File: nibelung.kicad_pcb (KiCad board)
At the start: 2 copper layers, 35.6 x 35.6 mm, 48 parts, among them J1 JST_PH_01x02, J2 JST_PH_01x02, J3 AudioJack3-TSW, J4 ScrewTerm_01x08_2.54mm, J5 ScrewTerm_01x08_2.54mm, J6 JST_SH_01x03, J7 JST_SH_01x03, U1 74HCT245, U2 LTC2850xS8, U3 Teensy4.0

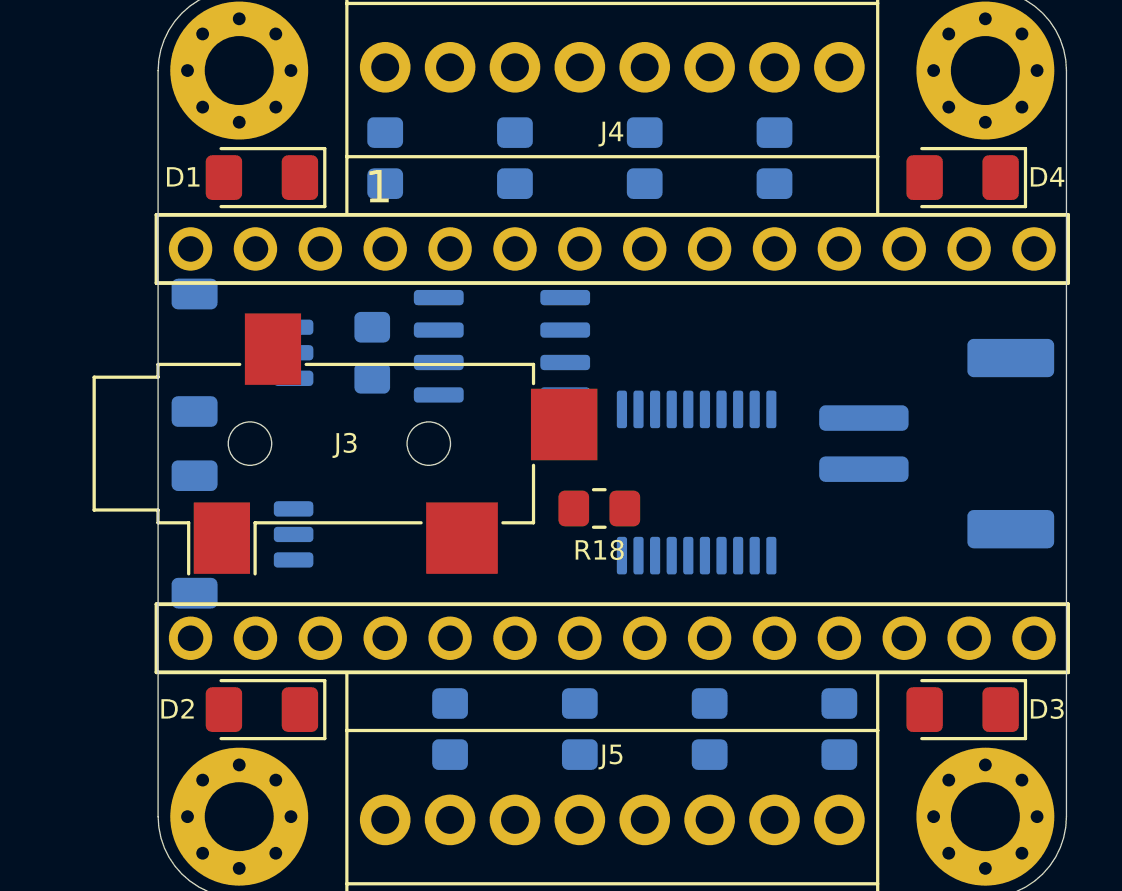
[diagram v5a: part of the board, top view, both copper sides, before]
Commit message: Revise placement and label output connections
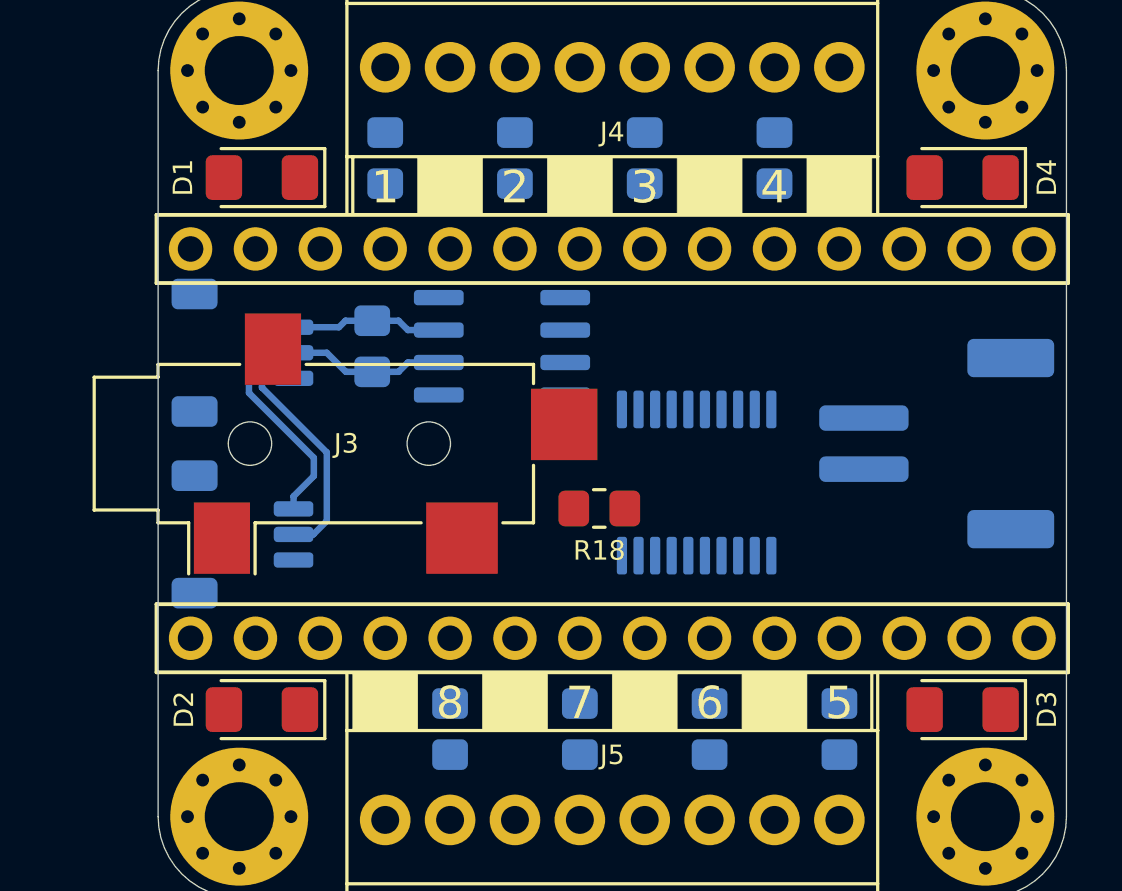
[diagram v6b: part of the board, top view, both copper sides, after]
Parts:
- moved R1 0.25 mm to (111.3, 97.8)
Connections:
- J6 pad 1: /A -> GND
- J6 pad 2: GND -> /A
- J7 pad 1: /A -> GND
- J7 pad 2: GND -> /A
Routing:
- net /A: track 0.00 -> 16.4 mm
- net /B: track 0.00 -> 15.7 mm
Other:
- net class Minimum added: clearance 0.1524, trace_width 0.1524, via_dia 0.508, via_drill 0.254
- net class Thin added: clearance 0.2032, trace_width 0.2032, via_dia 0.6096, via_drill 0.3048
- board text added: "2"
- board text added: "3"
- board text added: "4"
- board text added: "5"
- board text added: "6"
- board text added: "7"
- board text added: "8"
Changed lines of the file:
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@@
   (general
     (thickness 1.6)
-    (drawings 19)
-    (tracks 0)
+    (drawings 44)
+    (tracks 26)
     (zones 0)
     (modules 48)
@@
   (setup
     (last_trace_width 0.254)
+    (user_trace_width 0.1524)
+    (user_trace_width 0.2032)
+    (user_trace_width 0.254)
+    (user_trace_width 0.508)
+    (user_trace_width 0.635)
+    (user_trace_width 0.762)
+    (user_trace_width 1.27)
     (trace_clearance 0.254)
     (zone_clearance 0.508)
@@
     (via_min_size 0.508)
     (via_min_drill 0.254)
-    (uvia_size 0.6096)
-    (uvia_drill 0.3048)
+    (user_via 0.508 0.254)
+    (user_via 0.6096 0.3048)
+    (user_via 0.762 0.381)
+    (user_via 1.016 0.508)
+    (uvia_size 0.762)
+    (uvia_drill 0.381)
     (uvias_allowed no)
     (uvia_min_size 0)
@@
     (pad_to_mask_clearance 0.0508)
     (aux_axis_origin 0 0)
+    (grid_origin 104.14 109.22)
     (visible_elements 7FFFFFFF)
     (pcbplotparams
@@
     (via_dia 0.762)
     (via_drill 0.381)
-    (uvia_dia 0.6096)
-    (uvia_drill 0.3048)
+    (uvia_dia 0.762)
+    (uvia_drill 0.381)
     (diff_pair_width 0.254)
     (diff_pair_gap 0.254)
@@
     (add_net VIN)
   )
+  (net_class Minimum ""
+    (clearance 0.1524)
+    (trace_width 0.1524)
+    (via_dia 0.508)
+    (via_drill 0.254)
+    (uvia_dia 0.508)
+    (uvia_drill 0.254)
+    (diff_pair_width 0.1524)
+    (diff_pair_gap 0.1524)
+  )
+  (net_class Thin ""
+    (clearance 0.2032)
+    (trace_width 0.2032)
+    (via_dia 0.6096)
+    (via_drill 0.3048)
+    (uvia_dia 0.6096)
+    (uvia_drill 0.3048)
+    (diff_pair_width 0.2032)
+    (diff_pair_gap 0.2032)
+  )
   (module nibelung:Teensy40_Socket locked (layer F.Cu)
     (at 104.14 101.6 90)
@@
     (tags "LED handsolder")
     (attr smd)
-    (fp_text reference D4 (at -3.302 0) (layer F.SilkS)
+    (fp_text reference D4 (at -3.302 0 90) (layer F.SilkS)
       (effects (font (size 0.762 0.762) (thickness 0.127)))
     )
@@
     (tags "LED handsolder")
     (attr smd)
-    (fp_text reference D3 (at -3.302 0) (layer F.SilkS)
+    (fp_text reference D3 (at -3.302 0 90) (layer F.SilkS)
       (effects (font (size 0.762 0.762) (thickness 0.127)))
     )
@@
     (tags "LED handsolder")
     (attr smd)
-    (fp_text reference D2 (at 3.302 0) (layer F.SilkS)
+    (fp_text reference D2 (at 3.048 0 90) (layer F.SilkS)
       (effects (font (size 0.762 0.762) (thickness 0.127)))
     )
@@
     (tags "LED handsolder")
     (attr smd)
-    (fp_text reference D1 (at 3.0845 0 180) (layer F.SilkS)
+    (fp_text reference D1 (at 3.0845 0 270) (layer F.SilkS)
       (effects (font (size 0.762 0.762) (thickness 0.127)))
     )
@@
       (net 17 /B))
     (pad 2 smd roundrect (at 0 2 90) (size 0.6 1.55) (layers B.Cu B.Paste B.Mask) (roundrect_rratio 0.25)
-      (net 2 GND))
+      (net 18 /A))
     (pad 1 smd roundrect (at -1 2 90) (size 0.6 1.55) (layers B.Cu B.Paste B.Mask) (roundrect_rratio 0.25)
-      (net 18 /A))
+      (net 2 GND))
     (model ${KIPRJMOD}/footprints/.local/nibelung.3dshapes/SM03B-SRSS-TB.STEP
       (offset (xyz 0 1.27 -0.3048))
@@
       (net 17 /B))
     (pad 2 smd roundrect (at 0 2 90) (size 0.6 1.55) (layers B.Cu B.Paste B.Mask) (roundrect_rratio 0.25)
-      (net 2 GND))
+      (net 18 /A))
     (pad 1 smd roundrect (at -1 2 90) (size 0.6 1.55) (layers B.Cu B.Paste B.Mask) (roundrect_rratio 0.25)
-      (net 18 /A))
+      (net 2 GND))
     (model ${KIPRJMOD}/footprints/.local/nibelung.3dshapes/SM03B-SRSS-TB.STEP
       (offset (xyz 0 1.27 -0.3048))
@@
   )
   (module Resistor_SMD:R_0805_2012Metric_Pad1.20x1.40mm_HandSolder (layer B.Cu)
-    (at 111.252 98.044 90)
+    (at 111.252 97.79 90)
     (descr "Resistor SMD 0805 (2012 Metric), square (rectangular) end terminal, IPC_7351 nominal with elongated pad for handsoldering. (Body size source: IPC-SM-782 page 72, https://www.pcb-3d.com/wordpress/wp-content/uploads/ipc-sm-782a_amendment_1_and_2.pdf), generated with kicad-footprint-generator")
     (tags "resistor handsolder")
@@
     )
   )
+  (gr_text G (at 127 111.76) (layer Eco1.User)
+    (effects (font (size 1.27 1.27) (thickness 0.254)))
+  )
+  (gr_text G (at 121.92 111.76) (layer Eco1.User)
+    (effects (font (size 1.27 1.27) (thickness 0.254)))
+  )
+  (gr_text G (at 116.84 111.76) (layer Eco1.User)
+    (effects (font (size 1.27 1.27) (thickness 0.254)))
+  )
+  (gr_text G (at 111.76 111.76) (layer Eco1.User)
+    (effects (font (size 1.27 1.27) (thickness 0.254)))
+  )
+  (gr_text 5 (at 129.54 111.76) (layer F.SilkS)
+    (effects (font (size 1.27 1.27) (thickness 0.254)))
+  )
+  (gr_text 6 (at 124.46 111.76) (layer F.SilkS)
+    (effects (font (size 1.27 1.27) (thickness 0.254)))
+  )
+  (gr_text 7 (at 119.38 111.76) (layer F.SilkS)
+    (effects (font (size 1.27 1.27) (thickness 0.254)))
+  )
+  (gr_text 8 (at 114.3 111.76) (layer F.SilkS)
+    (effects (font (size 1.27 1.27) (thickness 0.254)))
+  )
+  (gr_poly (pts (xy 130.81 92.6465) (xy 128.27 92.6465) (xy 128.27 90.3605) (xy 130.81 90.3605)) (layer F.SilkS) (width 0.0254))
+  (gr_line (start 130.81 112.832) (end 130.81 110.5662) (layer F.SilkS) (width 0.127))
+  (gr_line (start 110.49 90.368) (end 110.49 92.6338) (layer F.SilkS) (width 0.127))
+  (gr_poly (pts (xy 110.49 110.5535) (xy 113.03 110.5535) (xy 113.03 112.8395) (xy 110.49 112.8395)) (layer F.SilkS) (width 0.0254))
+  (gr_poly (pts (xy 115.57 110.5535) (xy 118.11 110.5535) (xy 118.11 112.8395) (xy 115.57 112.8395)) (layer F.SilkS) (width 0.0254))
+  (gr_poly (pts (xy 120.65 110.5535) (xy 123.19 110.5535) (xy 123.19 112.8395) (xy 120.65 112.8395)) (layer F.SilkS) (width 0.0254))
+  (gr_poly (pts (xy 125.73 110.5535) (xy 128.27 110.5535) (xy 128.27 112.8395) (xy 125.73 112.8395)) (layer F.SilkS) (width 0.0254))
+  (gr_text G (at 129.54 91.567) (layer Eco1.User)
+    (effects (font (size 1.27 1.27) (thickness 0.254)))
+  )
+  (gr_text G (at 124.46 91.567) (layer Eco1.User)
+    (effects (font (size 1.27 1.27) (thickness 0.254)))
+  )
+  (gr_text G (at 119.38 91.567) (layer Eco1.User)
+    (effects (font (size 1.27 1.27) (thickness 0.254)))
+  )
+  (gr_text G (at 114.3 91.567) (layer Eco1.User)
+    (effects (font (size 1.27 1.27) (thickness 0.254)))
+  )
+  (gr_poly (pts (xy 125.73 92.6465) (xy 123.19 92.6465) (xy 123.19 90.3605) (xy 125.73 90.3605)) (layer F.SilkS) (width 0.0254))
+  (gr_poly (pts (xy 120.65 92.6465) (xy 118.11 92.6465) (xy 118.11 90.3605) (xy 120.65 90.3605)) (layer F.SilkS) (width 0.0254))
+  (gr_poly (pts (xy 115.57 92.6465) (xy 113.03 92.6465) (xy 113.03 90.3605) (xy 115.57 90.3605)) (layer F.SilkS) (width 0.0254))
+  (gr_text 4 (at 127 91.567) (layer F.SilkS)
+    (effects (font (size 1.27 1.27) (thickness 0.254)))
+  )
+  (gr_text 3 (at 121.92 91.567) (layer F.SilkS)
+    (effects (font (size 1.27 1.27) (thickness 0.254)))
+  )
+  (gr_text 2 (at 116.84 91.567) (layer F.SilkS)
+    (effects (font (size 1.27 1.27) (thickness 0.254)))
+  )
   (gr_text B (at 109.728 104.14 90) (layer B.SilkS)
     (effects (font (size 0.762 0.762) (thickness 0.127)) (justify mirror))
@@
   (gr_line (start 131.04 90.368) (end 131.04 92.6338) (layer F.SilkS) (width 0.127))
   (gr_line (start 110.26 90.368) (end 110.26 92.6338) (layer F.SilkS) (width 0.127))
-  (gr_text 1 (at 111.506 91.567) (layer F.SilkS)
+  (gr_text 1 (at 111.76 91.567) (layer F.SilkS)
     (effects (font (size 1.27 1.27) (thickness 0.254)))
   )
@@
   (gr_line (start 106.045 83.82) (end 135.255 83.82) (layer Edge.Cuts) (width 0.0508))
   (gr_line (start 102.87 116.205) (end 102.87 86.995) (layer Edge.Cuts) (width 0.0508))
+  (segment (start 113.857 97.155) (end 112.649 97.155) (width 0.254) (layer B.Cu) (net 17))
+  (segment (start 112.284 96.79) (end 111.252 96.79) (width 0.254) (layer B.Cu) (net 17))
+  (segment (start 112.649 97.155) (end 112.284 96.79) (width 0.254) (layer B.Cu) (net 17))
+  (segment (start 108.172 97.044) (end 109.95 97.044) (width 0.254) (layer B.Cu) (net 17))
+  (segment (start 110.204 96.79) (end 111.252 96.79) (width 0.254) (layer B.Cu) (net 17))
+  (segment (start 109.95 97.044) (end 110.204 96.79) (width 0.254) (layer B.Cu) (net 17))
+  (segment (start 108.172 103.664) (end 108.172 104.156) (width 0.254) (layer B.Cu) (net 17))
+  (segment (start 108.966 102.87) (end 108.172 103.664) (width 0.254) (layer B.Cu) (net 17))
+  (segment (start 108.966 102.156) (end 108.966 102.87) (width 0.254) (layer B.Cu) (net 17))
+  (segment (start 106.426 99.616) (end 108.966 102.156) (width 0.254) (layer B.Cu) (net 17))
+  (segment (start 107.172 97.044) (end 106.426 97.79) (width 0.254) (layer B.Cu) (net 17))
+  (segment (start 106.426 97.79) (end 106.426 99.616) (width 0.254) (layer B.Cu) (net 17))
+  (segment (start 108.172 97.044) (end 107.172 97.044) (width 0.254) (layer B.Cu) (net 17))
+  (segment (start 113.857 98.425) (end 112.649 98.425) (width 0.254) (layer B.Cu) (net 18))
+  (segment (start 112.284 98.79) (end 111.252 98.79) (width 0.254) (layer B.Cu) (net 18))
+  (segment (start 112.649 98.425) (end 112.284 98.79) (width 0.254) (layer B.Cu) (net 18))
+  (segment (start 108.947 105.156) (end 108.172 105.156) (width 0.254) (layer B.Cu) (net 18))
+  (segment (start 109.474011 104.628989) (end 108.947 105.156) (width 0.254) (layer B.Cu) (net 18))
+  (segment (start 109.474011 101.945575) (end 109.474011 104.628989) (width 0.254) (layer B.Cu) (net 18))
+  (segment (start 106.934 99.405564) (end 109.474011 101.945575) (width 0.254) (layer B.Cu) (net 18))
+  (segment (start 106.934 98.298) (end 106.934 99.405564) (width 0.254) (layer B.Cu) (net 18))
+  (segment (start 107.188 98.044) (end 106.934 98.298) (width 0.254) (layer B.Cu) (net 18))
+  (segment (start 108.172 98.044) (end 107.188 98.044) (width 0.254) (layer B.Cu) (net 18))
+  (segment (start 109.474 98.044) (end 108.172 98.044) (width 0.254) (layer B.Cu) (net 18))
+  (segment (start 110.22 98.79) (end 109.474 98.044) (width 0.254) (layer B.Cu) (net 18))
+  (segment (start 111.252 98.79) (end 110.22 98.79) (width 0.254) (layer B.Cu) (net 18))
 )

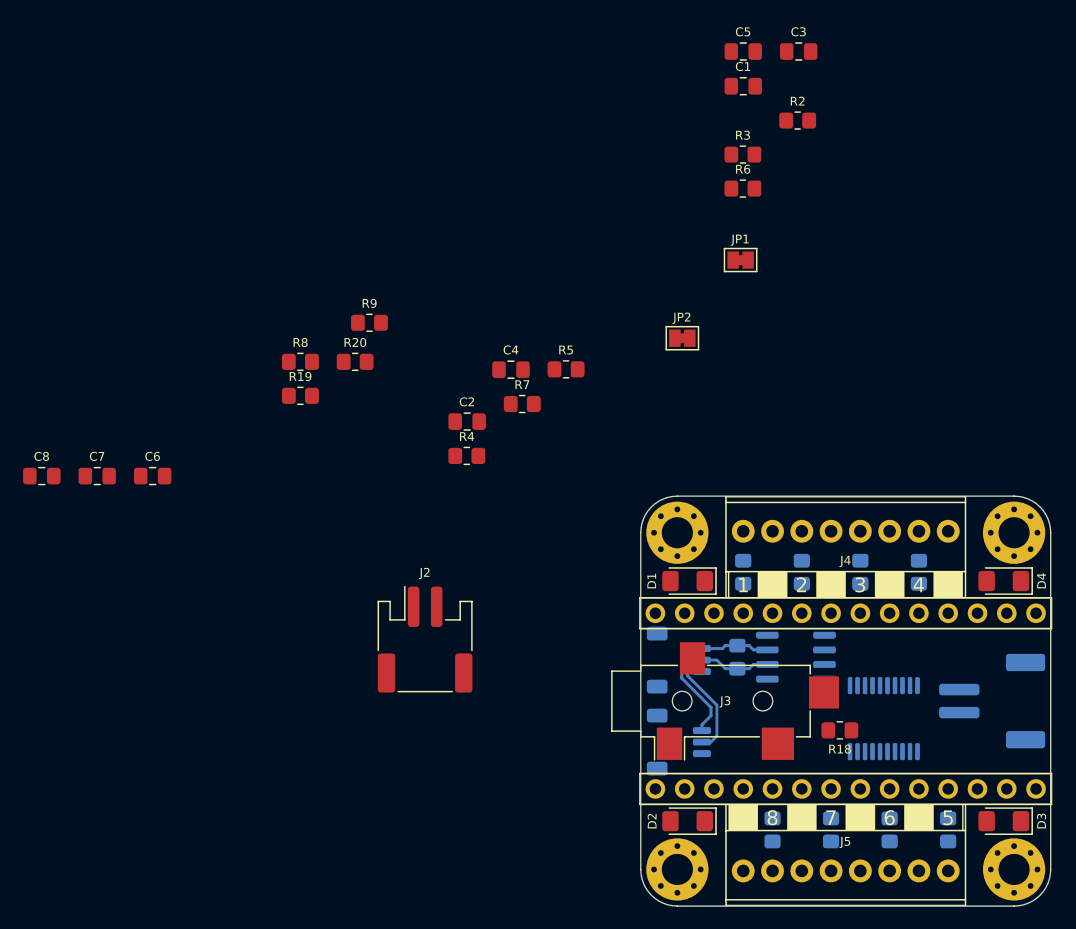
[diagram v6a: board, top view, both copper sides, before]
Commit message: Replace 2-pin PH power connector with 3-pin PH
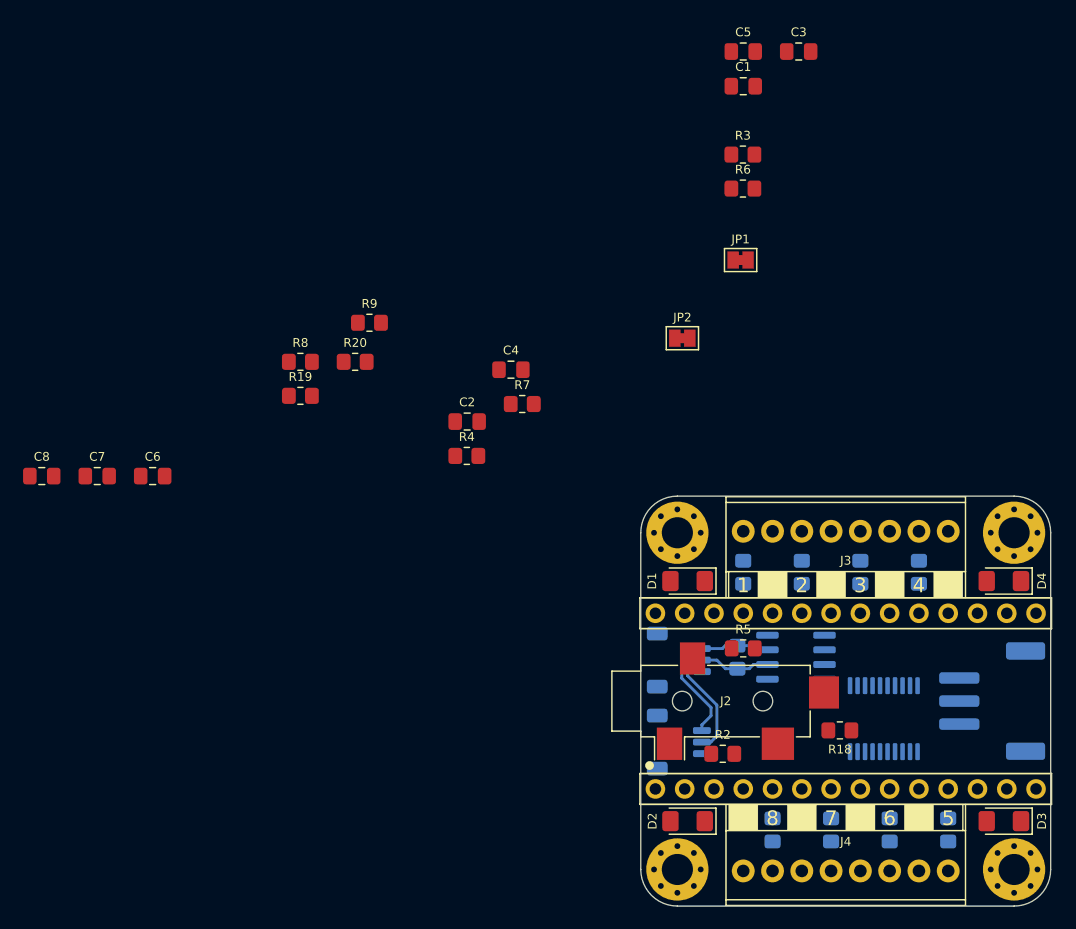
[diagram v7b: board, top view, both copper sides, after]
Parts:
- removed the J2 at (84.2, 96.3)
- J1: value JST_PH_01x02 -> JST_SH_01x03; footprint Connector_JST:JST_PH_S2B-PH-SM4-TB_1x02-1MP_P2.00mm_Horizontal -> Connector_JST:JST_PH_S3B-PH-SM4-TB_1x03-1MP_P2.00mm_Horizontal
- moved R2 55.3 mm to (110.0, 106.2)
- moved R5 28.7 mm to (111.8, 97.0)
- renumbered J3 to J2, J4 to J3, J5 to J4, J6 to J5, J7 to J6
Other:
- board text added: "5V"
- board text added: "GND"
- board text added: "VIN"
